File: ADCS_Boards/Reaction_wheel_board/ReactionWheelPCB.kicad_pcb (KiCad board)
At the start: 4 copper layers, 90.2 x 95.9 mm, 13 parts, among them J1 PC104_Connector, U1 Conn_1, U2 Conn_1, U3 Controller 1, U4 Controller 2, U5 Controller 3, U6 Controller 4, U7 Conn_1, U8 Conn_1

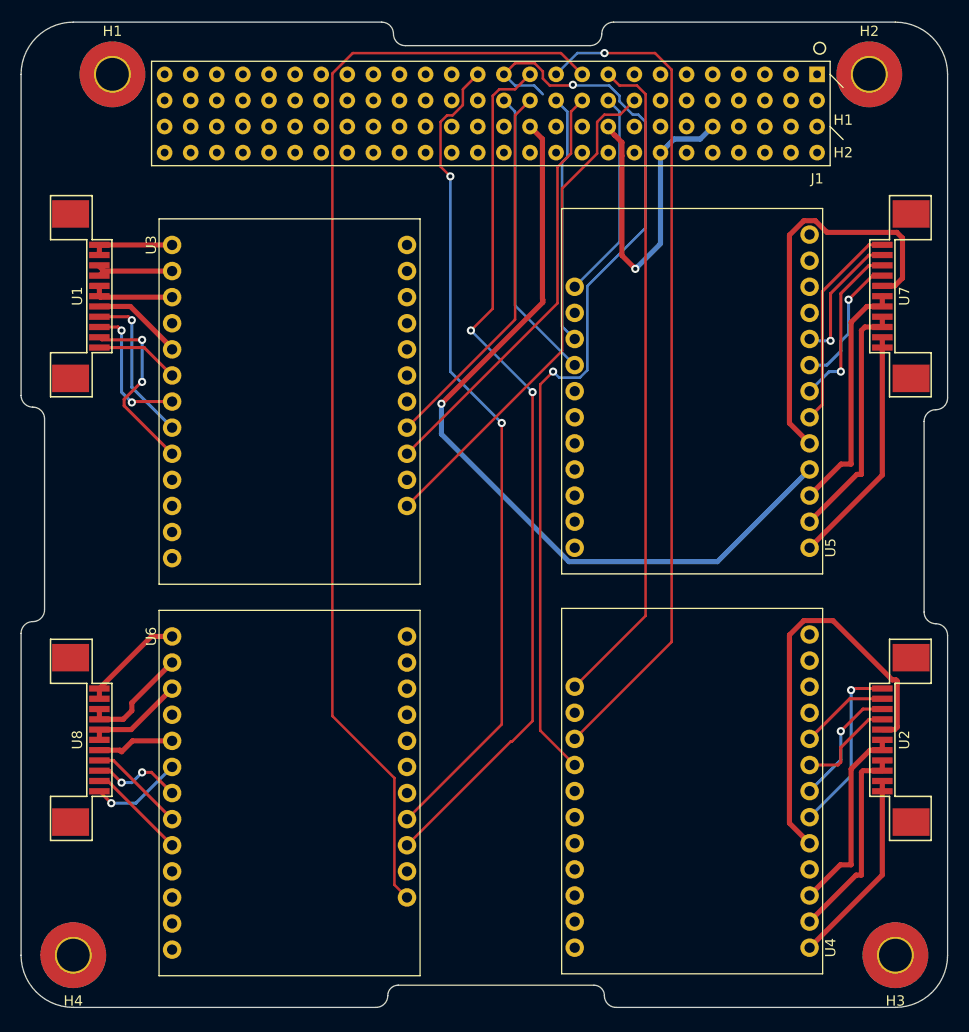
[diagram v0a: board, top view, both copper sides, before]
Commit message: adcs: updated reaction wheel board from Yasin
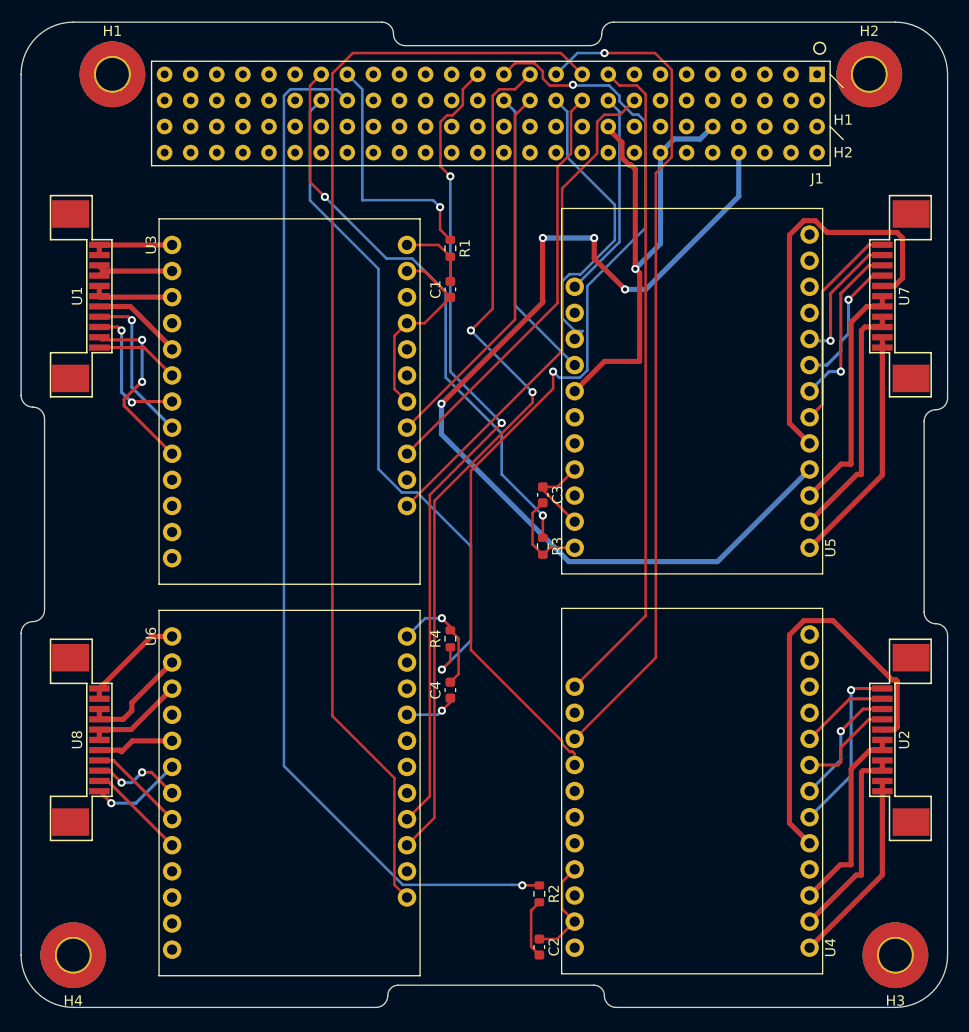
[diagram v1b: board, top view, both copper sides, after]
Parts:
- added C1: 10n, Capacitor_SMD:C_0603_1608Metric, F.Cu at (151.0, 73.0)
- added C2: 10n, Capacitor_SMD:C_0603_1608Metric, F.Cu at (159.7, 137.0)
- added C3: 10n, Capacitor_SMD:C_0603_1608Metric, F.Cu at (160.0, 93.0)
- added C4: 10n, Capacitor_SMD:C_0603_1608Metric, F.Cu at (151.0, 112.0)
- added R1: 10k, Resistor_SMD:R_0603_1608Metric, F.Cu at (151.0, 69.0)
- added R2: 10k, Resistor_SMD:R_0603_1608Metric, F.Cu at (159.7, 131.8)
- added R3: 10k, Resistor_SMD:R_0603_1608Metric, F.Cu at (160.0, 98.0)
- added R4: 10k, Resistor_SMD:R_0603_1608Metric, F.Cu at (151.0, 107.0)
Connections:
- J1 pad 60: unconnected-(J1-Pad60) -> +12V
- J1 pad 75: +12V -> unconnected-(J1-Pad75)
- U3 pad 24: unconnected-(U3-Pad24) -> RampControl(S1)_RLC
- U4 pad 24: unconnected-(U4-Pad24) -> RampControl(S2)_RLC
- U5 pad 24: unconnected-(U5-Pad24) -> RampControl(S3)_RLC
- U6 pad 24: unconnected-(U6-Pad24) -> RampControl(S4)_RLC
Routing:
- net RampControl(S2): track 0.00 -> 101.8 mm, vias 0 -> 1
- net RampControl(S4): track 0.00 -> 66.9 mm, vias 0 -> 1
- net GND: track 130.0 -> 189.8 mm, vias 1 -> 2
- net RampControl(S3): track 0.00 -> 56.4 mm, vias 0 -> 2
- net RampControl(S1): track 0.00 -> 24.3 mm, vias 0 -> 1
- net +12V: track 79.2 -> 98.2 mm, vias 1 -> 4
- net RampControl(S4)_RLC: track 0.00 -> 11.4 mm, vias 0 -> 1
- net RampControl(S3)_RLC: track 0.00 -> 9.26 mm
- net RampControl(S1)_RLC: track 0.00 -> 7.10 mm
- net RampControl(S2)_RLC: track 0.00 -> 5.79 mm
- net Direction(S3): track 24.4 -> 30.0 mm
- net PWM-SetValue(S2): track 92.6 -> 93.7 mm

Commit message: adcs: updated reaction wheel board from Yasin
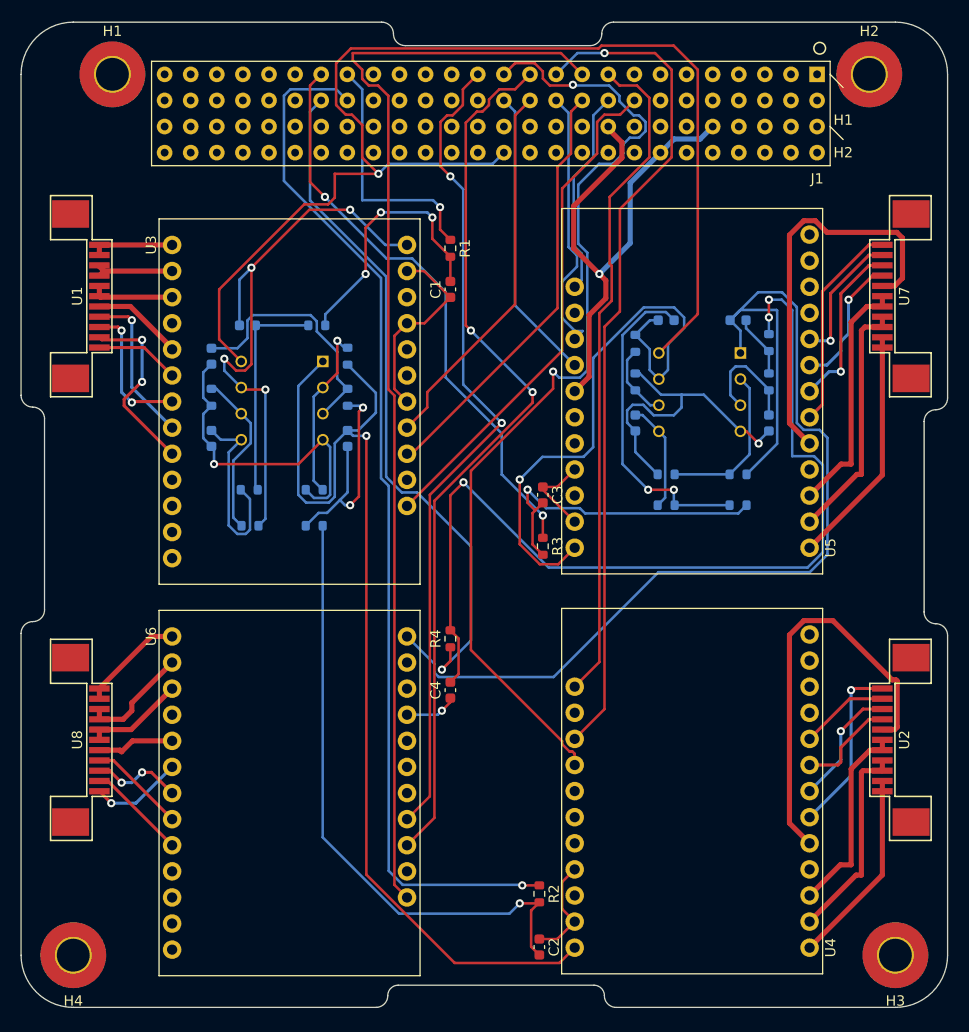
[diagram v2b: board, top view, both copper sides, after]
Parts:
- added C10: C, Capacitor_SMD:C_0603_1608Metric, B.Cu at (172.0, 76.0)
- added C11: C, Capacitor_SMD:C_0603_1608Metric, B.Cu at (127.8, 87.5)
- added C12: C, Capacitor_SMD:C_0603_1608Metric, B.Cu at (131.2, 76.5)
- added C5: C, Capacitor_SMD:C_0603_1608Metric, B.Cu at (179.0, 76.0)
- added C6: C, Capacitor_SMD:C_0603_1608Metric, B.Cu at (182.0, 86.0)
- added C7: C, Capacitor_SMD:C_0603_1608Metric, B.Cu at (141.0, 87.5)
- added C8: C, Capacitor_SMD:C_0603_1608Metric, B.Cu at (127.8, 79.5)
- added C9: C, Capacitor_SMD:C_0603_1608Metric, B.Cu at (169.0, 86.0)
- added R10: R, Resistor_SMD:R_0603_1608Metric, B.Cu at (127.8, 83.5)
- added R11: R, Resistor_SMD:R_0603_1608Metric, B.Cu at (131.5, 96.0)
- added R12: R, Resistor_SMD:R_0603_1608Metric, B.Cu at (141.0, 83.5)
- added R13: R, Resistor_SMD:R_0603_1608Metric, B.Cu at (172.0, 94.0)
- added R14: R, Resistor_SMD:R_0603_1608Metric, B.Cu at (179.0, 91.0)
- added R15: R, Resistor_SMD:R_0603_1608Metric, B.Cu at (172.0, 91.0)
- added R16: R, Resistor_SMD:R_0603_1608Metric, B.Cu at (131.4, 92.5)
- added R17: R, Resistor_SMD:R_0603_1608Metric, B.Cu at (141.0, 79.5)
- added R18: R, Resistor_SMD:R_0603_1608Metric, B.Cu at (137.8, 92.5)
- added R19: R, Resistor_SMD:R_0603_1608Metric, B.Cu at (179.0, 94.0)
- added R20: R, Resistor_SMD:R_0603_1608Metric, B.Cu at (138.0, 76.5)
- added R5: R, Resistor_SMD:R_0603_1608Metric, B.Cu at (182.0, 78.2)
- added R6: R, Resistor_SMD:R_0603_1608Metric, B.Cu at (137.8, 96.0)
- added R7: R, Resistor_SMD:R_0603_1608Metric, B.Cu at (169.0, 82.0)
- added R8: R, Resistor_SMD:R_0603_1608Metric, B.Cu at (169.0, 78.2)
- added R9: R, Resistor_SMD:R_0603_1608Metric, B.Cu at (182.0, 82.0)
- added U10: LM358, Footprints_QSAT:DIP794W45P254L959H508Q8, B.Cu at (134.6, 83.8)
- added U9: LM358, Footprints_QSAT:DIP794W45P254L959H508Q8, B.Cu at (175.3, 83.0)
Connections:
- C1 pad 2: RampControl(S1)_RLC -> RampControl(S1)_RC
- C2 pad 2: RampControl(S2)_RLC -> RampControl(S2)_RC
- C3 pad 2: RampControl(S3)_RLC -> RampControl(S3)_RC
- C4 pad 2: RampControl(S4)_RLC -> RampControl(S4)_RC
- R1 pad 2: RampControl(S1)_RLC -> RampControl(S1)_RC
- R2 pad 2: RampControl(S2)_RLC -> RampControl(S2)_RC
- R3 pad 2: RampControl(S3)_RLC -> RampControl(S3)_RC
- R4 pad 2: RampControl(S4)_RLC -> RampControl(S4)_RC
- U3 pad 24: RampControl(S1)_RLC -> RampControl(S1)_Out
- U4 pad 24: RampControl(S2)_RLC -> RampControl(S2)_Out
- U5 pad 24: RampControl(S3)_RLC -> RampControl(S3)_Out
- U6 pad 24: RampControl(S4)_RLC -> RampControl(S4)_Out
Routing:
- net +5V: track 0.00 -> 121.3 mm, vias 0 -> 1
- net RampControl(S4)_Out: track 0.00 -> 108.2 mm
- net RampControl(S2)_Out: track 0.00 -> 103.5 mm, vias 0 -> 1
- net +12V: track 98.2 -> 0.00 mm, vias 4 -> 0
- net RampControl(S4)_RC: track 0.00 -> 92.1 mm, vias 0 -> 3
- net GND: track 189.8 -> 253.5 mm, vias 2 -> 4
- net RampControl(S2)_RC: track 0.00 -> 60.7 mm, vias 0 -> 1
- net RampControl(S1)_Out: track 0.00 -> 57.2 mm, vias 0 -> 4
- net RampControl(S3)_Out: track 0.00 -> 56.6 mm, vias 0 -> 1
- net Net-(C10-Pad1): track 0.00 -> 31.8 mm, vias 0 -> 2
- net RampControl(S3)_RC: track 0.00 -> 30.8 mm, vias 0 -> 1
- net RampControl(S1)_RC: track 0.00 -> 25.4 mm, vias 0 -> 3
- net Net-(C8-Pad1): track 0.00 -> 24.1 mm
- net Net-(C7-Pad1): track 0.00 -> 22.7 mm, vias 0 -> 2
- net Net-(C12-Pad1): track 0.00 -> 21.2 mm
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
